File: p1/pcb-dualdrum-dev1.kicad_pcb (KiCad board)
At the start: 2 copper layers, 48 x 109.2 mm, 160 parts, among them P1 CONN-02x05, U1 072, U10 NJM, U11 072, U12 LM13700, U13 CD4001, U14 NJM, U15 NJM, U16 082, U17 082, U18 LM13700, U19 NJM, U2 CD4001, U20 NJM, U21 082, U22 082, U23 082, U3 LM13700, U4 NJM, U5 NJM, U6 082, U7 082, U8 LM13700, U9 NJM

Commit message: grouped components
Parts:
- removed U10, U14, U15, U19, U20: NJM, 4ms_Package_SSOP:TSSOP-8_4.4x3mm_Pitch0.65mm
- removed U11: 072, 4ms_Package_SSOP:TSSOP-8_4.4x3mm_Pitch0.65mm
- removed U12, U18: LM13700, 4ms_Package_SOIC:SOIC-16_3.9x9.9mm_Pitch1.27mm
- removed U13: CD4001, 4ms_Package_SOIC:SOIC-14_3.9x8.65mm_Pitch1.27mm
- removed U16, U17, U21, U22, U23: 082, 4ms_Package_SSOP:TSSOP-8_4.4x3mm_Pitch0.65mm
- added CD1: CD4001, 4ms_Package_SOIC:SOIC-14_3.9x8.65mm_Pitch1.27mm, F.Cu at (-38.0, -43.9)
- added CD2: CD4001, 4ms_Package_SOIC:SOIC-14_3.9x8.65mm_Pitch1.27mm, F.Cu at (82.9, -51.6)
- added LM1: LM13700, 4ms_Package_SOIC:SOIC-16_3.9x9.9mm_Pitch1.27mm, F.Cu at (77.2, -159.1)
- added LM2: LM13700, 4ms_Package_SOIC:SOIC-16_3.9x9.9mm_Pitch1.27mm, F.Cu at (77.2, -128.1)
- added LM3: LM13700, 4ms_Package_SOIC:SOIC-16_3.9x9.9mm_Pitch1.27mm, F.Cu at (-20.7, -164.0)
- added LM4: LM13700, 4ms_Package_SOIC:SOIC-16_3.9x9.9mm_Pitch1.27mm, F.Cu at (-22.5, -122.2)
- U1: value 072 -> 082
- U2: value CD4001 -> 082; footprint 4ms_Package_SOIC:SOIC-14_3.9x8.65mm_Pitch1.27mm -> 4ms_Package_SSOP:TSSOP-8_4.4x3mm_Pitch0.65mm
- U3: value LM13700 -> 082; footprint 4ms_Package_SOIC:SOIC-16_3.9x9.9mm_Pitch1.27mm -> 4ms_Package_SSOP:TSSOP-8_4.4x3mm_Pitch0.65mm
- U4, U5, U9: value NJM -> 082
- U8: value LM13700 -> 082-NJM; footprint 4ms_Package_SOIC:SOIC-16_3.9x9.9mm_Pitch1.27mm -> 4ms_Package_SSOP:TSSOP-8_4.4x3mm_Pitch0.65mm
- moved C36 390.5 mm to (66.2, -194.5)
- moved C40 389.7 mm to (-21.1, -184.0)
- moved R37 389.1 mm to (-35.5, -168.3)
- moved R12 388.9 mm to (83.0, -188.8)
- moved C41 388.8 mm to (-15.1, -182.4)
- moved C37 385.5 mm to (65.7, -190.2)
- moved R38 383.4 mm to (-11.7, -171.4)
- moved C23 381.5 mm to (-20.5, -171.9)
- moved R40 378.5 mm to (-35.3, -163.7)
- moved R34 374.8 mm to (-35.3, -171.8)
- moved R13 372.6 mm to (86.5, -189.4)
- moved R44 370.4 mm to (-34.9, -157.7)
- moved C27 368.3 mm to (-21.2, -156.9)
- moved R6 367.8 mm to (70.0, -172.6)
- moved R42 365.2 mm to (-11.8, -164.6)
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- renumbered FreqE to Freq2
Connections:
- D1 pad 1: Net-(D1-Pad1) -> Net-(CD1-Pad1)
- R1 pad 1: +9V -> +12V
- R10 pad 1: Net-(R10-Pad1) -> Net-(LM1-Pad13)
- R12 pad 1: Net-(R12-Pad1) -> Net-(LM1-Pad3)
- R13 pad 2: Net-(R13-Pad2) -> Net-(LM1-Pad4)
- R17 pad 2: Net-(R10-Pad1) -> Net-(LM1-Pad13)
- R21 pad 2: Net-(R10-Pad1) -> Net-(LM1-Pad13)
- R23 pad 2: Net-(R23-Pad2) -> Net-(LM2-Pad14)
- R25 pad 1: Net-(R23-Pad2) -> Net-(LM2-Pad14)
- R26 pad 2: Net-(R26-Pad2) -> Net-(LM2-Pad3)
- R27 pad 1: Net-(R27-Pad1) -> Net-(LM2-Pad13)
- R28 pad 1: Net-(R26-Pad2) -> Net-(LM2-Pad3)
- R29 pad 2: Net-(R29-Pad2) -> Net-(LM2-Pad4)
- R3 pad 2: Net-(D1-Pad1) -> Net-(CD1-Pad1)
- R30 pad 2: Net-(R27-Pad1) -> Net-(LM2-Pad13)
- R31 pad 2: Net-(R27-Pad1) -> Net-(LM2-Pad13)
- R32 pad 1: +9V -> +12V
- R4 pad 2: Net-(R4-Pad2) -> Net-(LM1-Pad14)
- R6 pad 1: Net-(R4-Pad2) -> Net-(LM1-Pad14)
- R7 pad 2: Net-(R12-Pad1) -> Net-(LM1-Pad3)
- R9 pad 2: Net-(R9-Pad2) -> Net-(CD1-Pad11)
- U1 pad 1: (no net) -> Net-(Bypass_2nd_Filter1-Pad2)
- U1 pad 2: (no net) -> Net-(Bypass_2nd_Filter1-Pad2)
- U1 pad 3: (no net) -> Net-(C4-Pad1)
- U1 pad 4: (no net) -> -12VA
- U1 pad 5: Net-(C1-Pad2) -> Net-(C5-Pad1)
- U1 pad 6: Net-(IN2-Pad3) -> Net-(R21-Pad1)
- U1 pad 7: Net-(IN2-Pad3) -> Net-(R21-Pad1)
- U1 pad 8: (no net) -> +12V
- U2 pad 1: Net-(D1-Pad1) -> Net-(Bypass_2nd_Filter1-Pad1)
- U2 pad 2: Net-(U2-Pad2) -> Net-(Bypass_2nd_Filter1-Pad1)
- U2 pad 3: Net-(C2-Pad1) -> Net-(C9-Pad1)
- U2 pad 4: Net-(U2-Pad2) -> -12VA
- U2 pad 5: Net-(C2-Pad2) -> Net-(C10-Pad1)
- U2 pad 6: Net-(C2-Pad2) -> Net-(R31-Pad1)
- U2 pad 7: GND -> Net-(R31-Pad1)
- U2 pad 8: Net-(U2-Pad2) -> +12V
- U3 pad 1: Net-(Freq1-Pad2) -> Net-(Bypass_2nd_Filter2-Pad2)
- U3 pad 2: Net-(U3-Pad2) -> Net-(Bypass_2nd_Filter2-Pad2)
- U3 pad 3: Net-(R12-Pad1) -> Net-(C14-Pad1)
- U3 pad 4: Net-(R13-Pad2) -> -12VA
- U3 pad 5: Net-(C5-Pad1) -> Net-(C15-Pad1)
- U3 pad 6: -12VA -> Net-(R50-Pad1)
- U3 pad 7: Net-(U3-Pad7) -> Net-(R50-Pad1)
- U3 pad 8: Net-(U3-Pad8) -> +12V
- U4 pad 1: Net-(Bypass_2nd_Filter1-Pad2) -> Net-(Bypass_2nd_Filter2-Pad1)
- U4 pad 2: Net-(Bypass_2nd_Filter1-Pad2) -> Net-(Bypass_2nd_Filter2-Pad1)
- U4 pad 3: Net-(C4-Pad1) -> Net-(C19-Pad1)
- U4 pad 5: GND -> Net-(C20-Pad1)
- U4 pad 6: Net-(C3-Pad1) -> Net-(R62-Pad1)
- U4 pad 7: Net-(C3-Pad2) -> Net-(R62-Pad1)
- U5 pad 1: Net-(R21-Pad1) -> Net-(IN2-Pad3)
- U5 pad 2: Net-(R21-Pad1) -> Net-(IN2-Pad3)
- U5 pad 3: Net-(C5-Pad1) -> Net-(C1-Pad2)
- U5 pad 5: GND -> Net-(C11-Pad2)
- U5 pad 6: Net-(C13-Pad1) -> Net-(R34-Pad1)
- U5 pad 7: Net-(C13-Pad2) -> Net-(R34-Pad1)
- U6 pad 1: Net-(C6-Pad2) -> Net-(R19-Pad2)
- U6 pad 2: Net-(R19-Pad1) -> Net-(R19-Pad2)
- U6 pad 3: GND -> Net-(Bypass_2nd_Filter1-Pad1)
- U6 pad 5: Net-(R16-Pad2) -> GND
- U6 pad 6: Net-(R14-Pad2) -> Net-(R19-Pad1)
- U6 pad 7: Net-(R14-Pad2) -> Net-(C6-Pad2)
- U7 pad 1: Net-(C16-Pad2) -> Net-(R48-Pad2)
- U7 pad 2: Net-(R48-Pad1) -> Net-(R48-Pad2)
- U7 pad 3: GND -> Net-(Bypass_2nd_Filter2-Pad1)
- U7 pad 5: Net-(Bypass_2nd_Filter1-Pad1) -> GND
- U7 pad 6: Net-(R19-Pad2) -> Net-(R48-Pad1)
- U7 pad 7: Net-(R19-Pad2) -> Net-(C16-Pad2)
- U8 pad 1: Net-(Freq1-Pad2) -> Net-(C3-Pad2)
- U8 pad 2: Net-(U8-Pad2) -> Net-(C3-Pad1)
- U8 pad 3: Net-(R26-Pad2) -> GND
- U8 pad 4: Net-(R29-Pad2) -> -12VA
- U8 pad 5: Net-(C10-Pad1) -> GND
- U8 pad 6: -12VA -> Net-(C13-Pad1)
- U8 pad 7: Net-(U8-Pad7) -> Net-(C13-Pad2)
- U8 pad 8: Net-(U8-Pad8) -> +12V
- U9 pad 1: Net-(Bypass_2nd_Filter1-Pad1) -> Net-(R14-Pad2)
- U9 pad 2: Net-(Bypass_2nd_Filter1-Pad1) -> Net-(R14-Pad2)
- U9 pad 3: Net-(C9-Pad1) -> Net-(R16-Pad2)
- U9 pad 4: (no net) -> -12VA
- U9 pad 5: (no net) -> Net-(R45-Pad1)
- U9 pad 6: (no net) -> Net-(R47-Pad2)
- U9 pad 7: (no net) -> Net-(R47-Pad2)
- U9 pad 8: (no net) -> +12V

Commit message: cruisin
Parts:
- moved P1 116.3 mm to (23.8, -46.6)
- moved C5 104.2 mm to (34.1, -98.3), turned to 180 degrees
- moved R13 103.7 mm to (34.1, -99.9)
- moved R7 101.2 mm to (34.1, -103.0)
- moved R12 100.1 mm to (34.1, -101.5), turned to 180 degrees
- moved U1 92.4 mm to (39.7, -106.2)
- moved C37 90.7 mm to (34.0, -105.2), turned to 180 degrees
- moved C36 89.6 mm to (45.3, -107.3)
- moved R34 86.8 mm to (17.8, -103.1), turned to 180 degrees
- moved C40 86.5 mm to (17.8, -106.8)
- moved R37 85.5 mm to (17.8, -101.5)
- moved C23 85.1 mm to (17.6, -95.8)
- moved C4 84.0 mm to (45.6, -98.1)
- moved R40 83.6 mm to (17.8, -99.2)
- moved R29 83.3 mm to (33.6, -75.8)
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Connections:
- C29 pad 1: Net-(C29-Pad1) -> +12V
- C31 pad 2: Net-(C31-Pad2) -> -12VA
- R19 pad 1: Net-(R19-Pad1) -> Net-(C6-Pad1)
- R48 pad 1: Net-(R48-Pad1) -> Net-(C16-Pad1)
- U1 pad 1: Net-(Bypass_2nd_Filter1-Pad2) -> Net-(R21-Pad1)
- U1 pad 2: Net-(Bypass_2nd_Filter1-Pad2) -> Net-(R21-Pad1)
- U1 pad 3: Net-(C4-Pad1) -> Net-(C5-Pad1)
- U1 pad 5: Net-(C5-Pad1) -> Net-(C4-Pad1)
- U1 pad 6: Net-(R21-Pad1) -> Net-(Bypass_2nd_Filter1-Pad2)
- U1 pad 7: Net-(R21-Pad1) -> Net-(Bypass_2nd_Filter1-Pad2)
- U2 pad 1: Net-(Bypass_2nd_Filter1-Pad1) -> Net-(R31-Pad1)
- U2 pad 2: Net-(Bypass_2nd_Filter1-Pad1) -> Net-(R31-Pad1)
- U2 pad 3: Net-(C9-Pad1) -> Net-(C10-Pad1)
- U2 pad 5: Net-(C10-Pad1) -> Net-(C9-Pad1)
- U2 pad 6: Net-(R31-Pad1) -> Net-(Bypass_2nd_Filter1-Pad1)
- U2 pad 7: Net-(R31-Pad1) -> Net-(Bypass_2nd_Filter1-Pad1)
- U3 pad 1: Net-(Bypass_2nd_Filter2-Pad2) -> Net-(R50-Pad1)
- U3 pad 2: Net-(Bypass_2nd_Filter2-Pad2) -> Net-(R50-Pad1)
- U3 pad 3: Net-(C14-Pad1) -> Net-(C15-Pad1)
- U3 pad 5: Net-(C15-Pad1) -> Net-(C14-Pad1)
- U3 pad 6: Net-(R50-Pad1) -> Net-(Bypass_2nd_Filter2-Pad2)
- U3 pad 7: Net-(R50-Pad1) -> Net-(Bypass_2nd_Filter2-Pad2)
- U4 pad 1: Net-(Bypass_2nd_Filter2-Pad1) -> Net-(R62-Pad1)
- U4 pad 2: Net-(Bypass_2nd_Filter2-Pad1) -> Net-(R62-Pad1)
- U4 pad 3: Net-(C19-Pad1) -> Net-(C20-Pad1)
- U4 pad 5: Net-(C20-Pad1) -> Net-(C19-Pad1)
- U4 pad 6: Net-(R62-Pad1) -> Net-(Bypass_2nd_Filter2-Pad1)
- U4 pad 7: Net-(R62-Pad1) -> Net-(Bypass_2nd_Filter2-Pad1)
- U6 pad 6: Net-(R19-Pad1) -> Net-(C6-Pad1)
- U7 pad 6: Net-(R48-Pad1) -> Net-(C16-Pad1)

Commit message: good stopping point
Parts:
- moved R53 19.3 mm to (54.4, -16.4)
- moved R18 16.0 mm to (-5.28, -16.1)
- moved P1 6.40 mm to (23.8, -40.2)
- moved GATE_LED2 2.46 mm to (36.5, -13.5)
- moved GATE_LED1 1.91 mm to (11.5, -13.5)
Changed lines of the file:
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@@
   )
   (module 4ms_Resistor:R_0603 (layer F.Cu)
-    (at 35.13 -14.62)
+    (at 54.35 -16.43)
     (descr "Resistor SMD 0603, reflow soldering, Vishay (see dcrcw.pdf)")
     (tags "resistor 0603")
@@
   )
   (module 4ms_Resistor:R_0603 (layer F.Cu)
-    (at 10.7 -14.59 180)
+    (at -5.28 -16.05 180)
     (descr "Resistor SMD 0603, reflow soldering, Vishay (see dcrcw.pdf)")
     (tags "resistor 0603")
@@
   )
   (module 4ms_Connector:Pins_2x05_2.54mm_TH_Europower (layer F.Cu)
-    (at 23.82 -46.64)
+    (at 23.75 -40.24)
     (tags "Through hole pin header THT 2x05 2.54mm Eurorack power europower")
     (fp_text reference P1 (at 0 -1.35 -90) (layer F.SilkS) hide
@@
   )
   (module 4ms_LED:LED_0603_1608Metric (layer B.Cu)
-    (at 35.23 -15.61 180)
+    (at 36.5 -13.5 180)
     (descr "LED SMD 0603 (1608 Metric), square (rectangular) end terminal, IPC_7351 nominal, (Body size source: http://www.tortai-tech.com/upload/download/2011102023233369053.pdf), generated with kicad-footprint-generator")
     (tags diode)
@@
   )
   (module 4ms_LED:LED_0603_1608Metric (layer B.Cu)
-    (at 10.82 -15.29 180)
+    (at 11.5 -13.5 180)
     (descr "LED SMD 0603 (1608 Metric), square (rectangular) end terminal, IPC_7351 nominal, (Body size source: http://www.tortai-tech.com/upload/download/2011102023233369053.pdf), generated with kicad-footprint-generator")
     (tags diode)

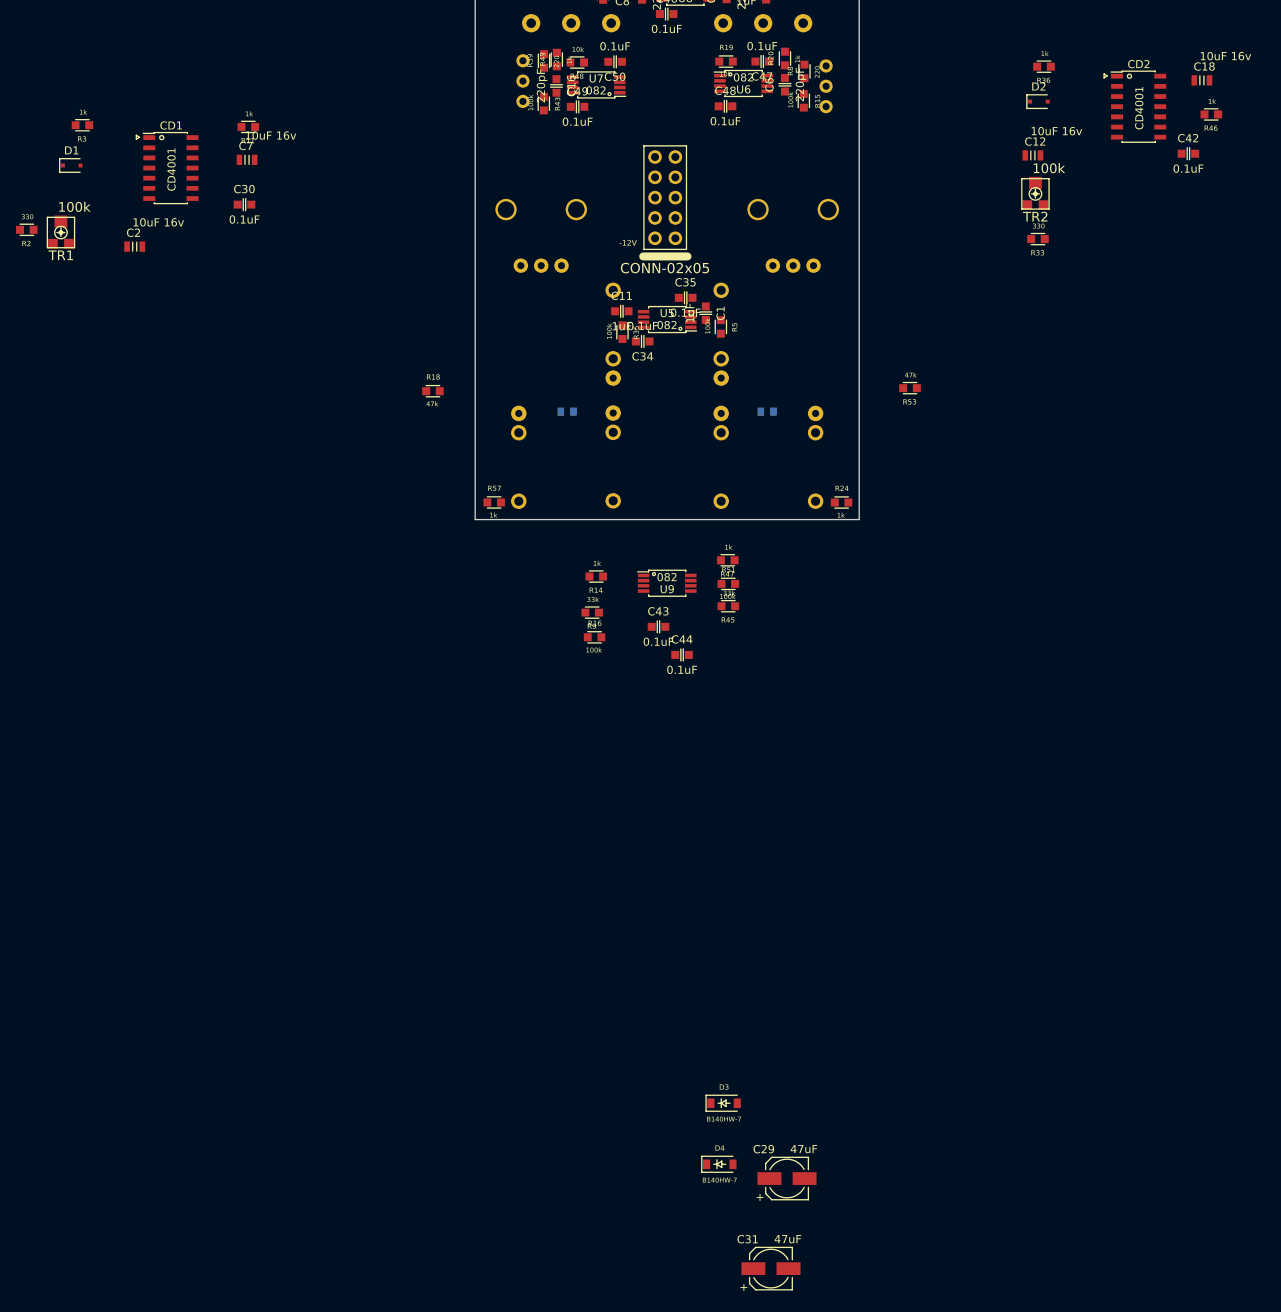
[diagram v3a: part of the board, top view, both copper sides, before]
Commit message: placed all components
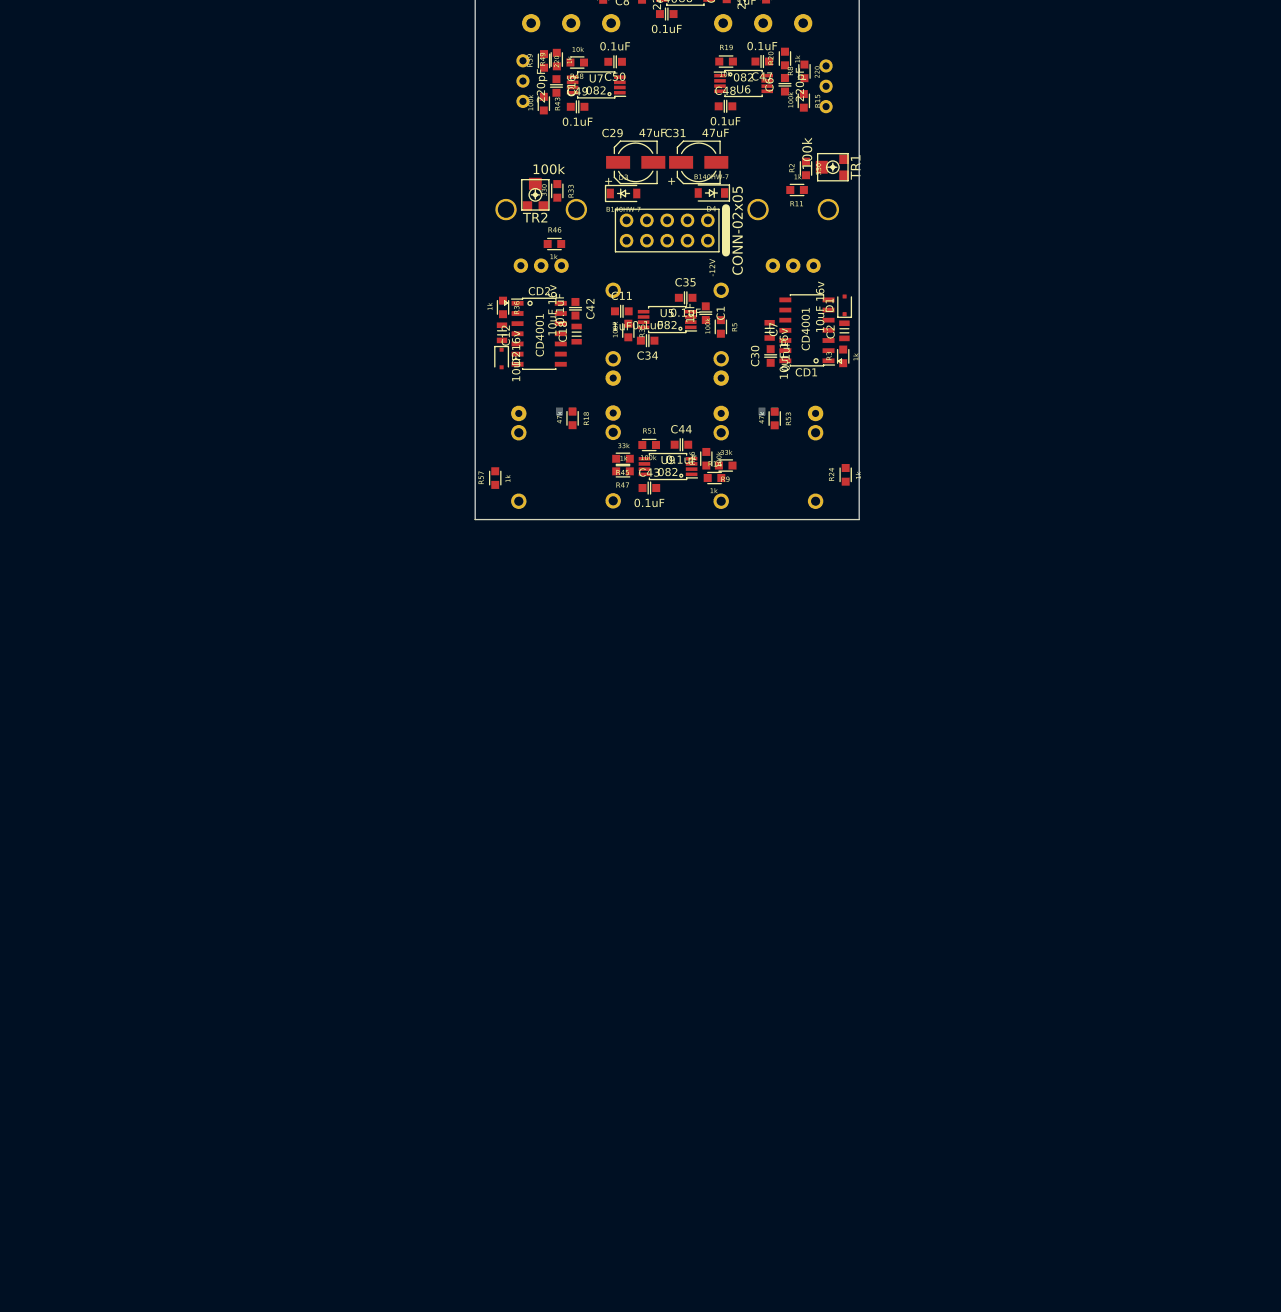
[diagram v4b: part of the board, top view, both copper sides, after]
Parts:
- moved C31 138.6 mm to (27.9, -44.6)
- moved C29 128.4 mm to (20.1, -44.6)
- moved D4 121.4 mm to (29.5, -40.8), turned to 180 degrees
- moved D3 114.4 mm to (18.5, -40.8)
- moved R3 99.4 mm to (46.0, -20.4), turned to 270 degrees
- moved D1 98.2 mm to (46.2, -26.8), turned to 90 degrees
- moved R2 97.7 mm to (41.4, -43.9), turned to 270 degrees
- moved TR1 96.8 mm to (44.7, -44.0), turned to 90 degrees
- moved C2 89.3 mm to (46.2, -23.6), turned to 90 degrees
- moved C18 84.4 mm to (12.7, -23.2), turned to 90 degrees
- moved R46 83.7 mm to (9.91, -34.4), turned to 180 degrees
- moved CD1 82.0 mm to (41.5, -23.7), turned to 180 degrees
- moved CD2 80.1 mm to (8.01, -23.2)
- moved C42 79.0 mm to (12.5, -26.4), turned to 270 degrees
- moved D2 74.4 mm to (3.30, -20.1), turned to 270 degrees
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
